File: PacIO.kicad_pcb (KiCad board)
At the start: 2 copper layers, 45.8 x 60 mm, 16 parts, among them J1 PacMan_Connector, J2 E-ink Display, J4 Charge_Indicator

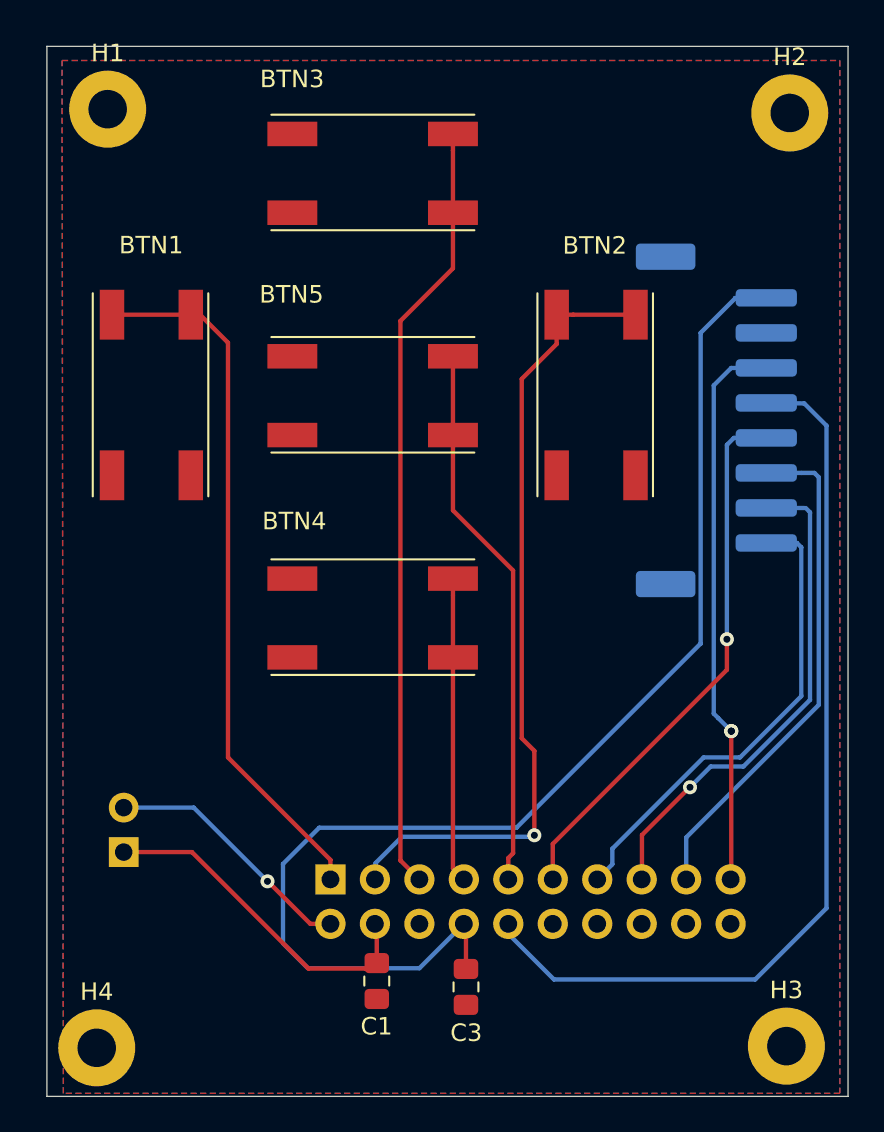
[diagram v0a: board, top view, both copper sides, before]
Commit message: Moved Parts Positions for final panel
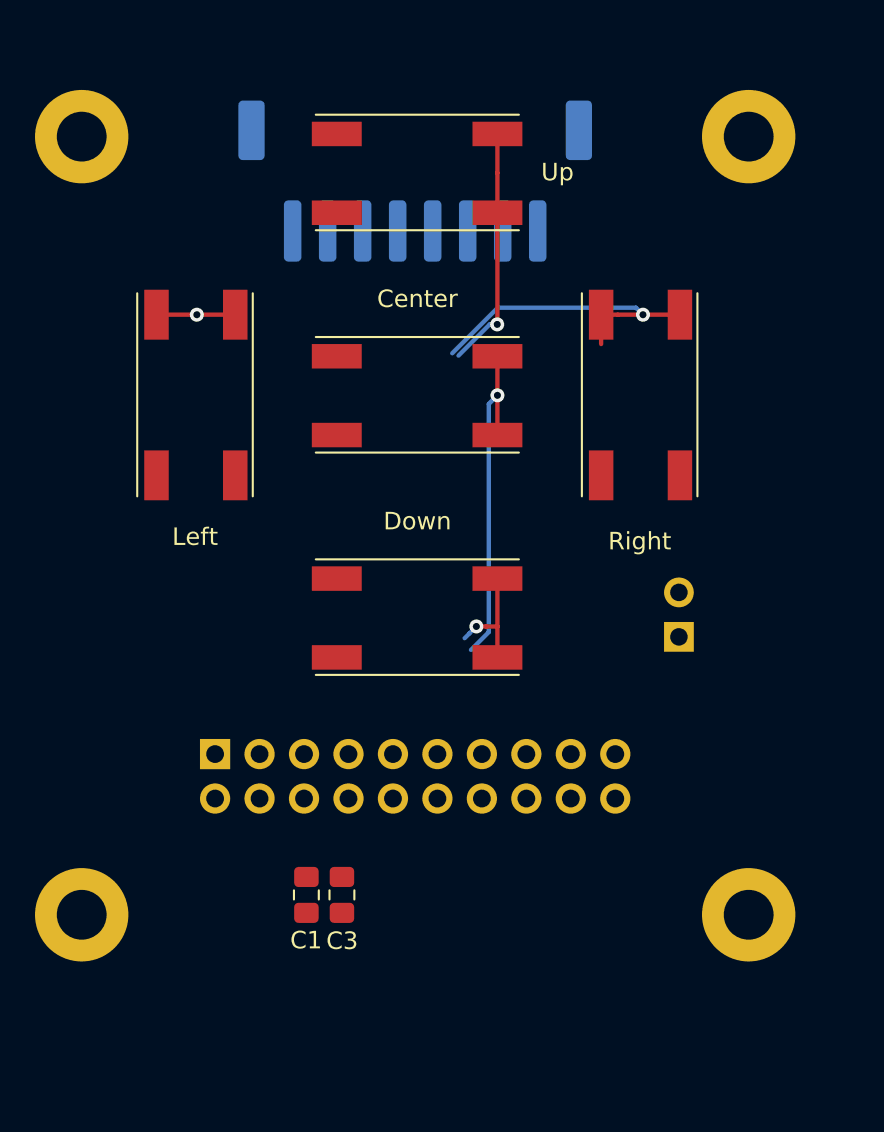
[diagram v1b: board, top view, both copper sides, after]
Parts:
- removed LOGO1: LafECEDepLogo, Lafayette_Electric_Car_Footprints:ECE_Logo_Jon
- H1, H2, H3, H4: footprint MountingHole:MountingHole_2.2mm_M2_Pad -> Lafayette_Electric_Car_Footprints:MountingHole_#4_Pad
- moved LOGO2 36.2 mm to (178.1, 109.3)
- moved J4 34.0 mm to (146.5, 126.4)
- moved J2 22.0 mm to (131.4, 100.3), turned to 0 degrees
- moved J1 9.73 mm to (120.0, 133.1)
- moved C3 8.82 mm to (127.3, 141.1)
- moved H3 7.81 mm to (150.5, 142.2)
- moved H4 7.65 mm to (112.4, 142.2)
- moved C1 6.35 mm to (125.2, 141.1)
- moved H2 2.71 mm to (150.5, 97.8)
- moved Center 2.54 mm to (131.6, 112.5)
- moved Down 2.54 mm to (131.6, 125.2)
- moved Up 2.54 mm to (131.6, 99.8)
- moved Left 2.54 mm to (118.9, 112.5)
- moved Right 2.54 mm to (144.3, 112.5)
- moved H1 2.16 mm to (112.4, 97.8)
- renumbered BTN5 to Center, BTN4 to Down, BTN1 to Left, BTN2 to Right, BTN3 to Up
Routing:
- net +3V3: track 70.6 -> 0.00 mm
- net /DISP_CLK: track 53.0 -> 0.00 mm
- net /BTN_LEFT: track 40.4 -> 5.03 mm, vias 0 -> 1
- net /DISP_DIN: track 32.8 -> 0.00 mm, vias 2 -> 0
- net /DISP_CS: track 31.4 -> 0.00 mm, vias 1 -> 0
- net /BTN_UP: track 44.3 -> 13.8 mm, vias 0 -> 1
- net /DISP_DC: track 29.2 -> 0.00 mm
- net /DISP_RST: track 28.5 -> 0.00 mm, vias 1 -> 0
- net /BTN_RIGHT: track 46.0 -> 18.3 mm
- net /DISP_BUSY: track 27.5 -> 0.00 mm
- net +24V: track 19.8 -> 0.00 mm
- net /CHRGE_LED: track 14.6 -> 0.00 mm, vias 1 -> 0
- net /BTN_CENTER: track 31.4 -> 19.7 mm, vias 0 -> 1
- net /BTN_DOWN: track 17.4 -> 6.63 mm, vias 0 -> 1
- removed copper zone on B.Cu, net GND
- removed copper zone on F.Cu, net GND
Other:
- board outline removed

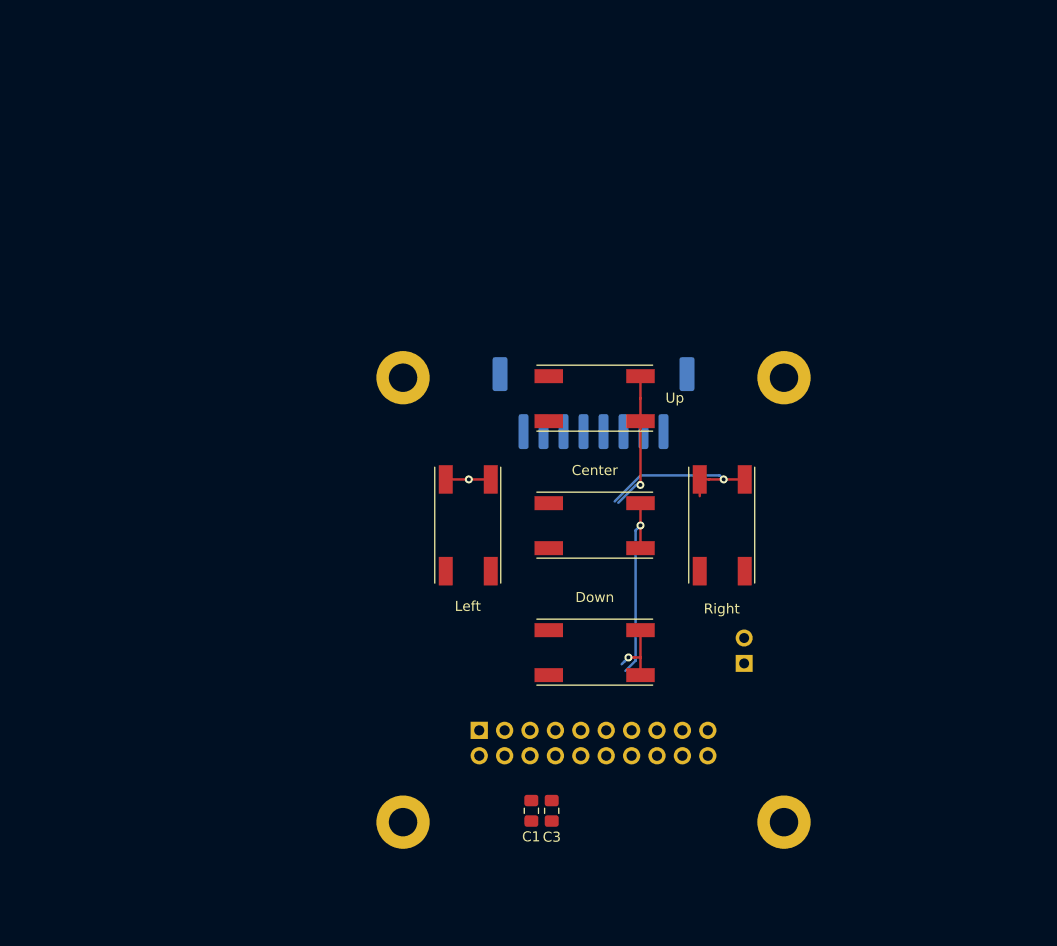
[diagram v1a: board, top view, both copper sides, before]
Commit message: Dimensions and Edge cuts
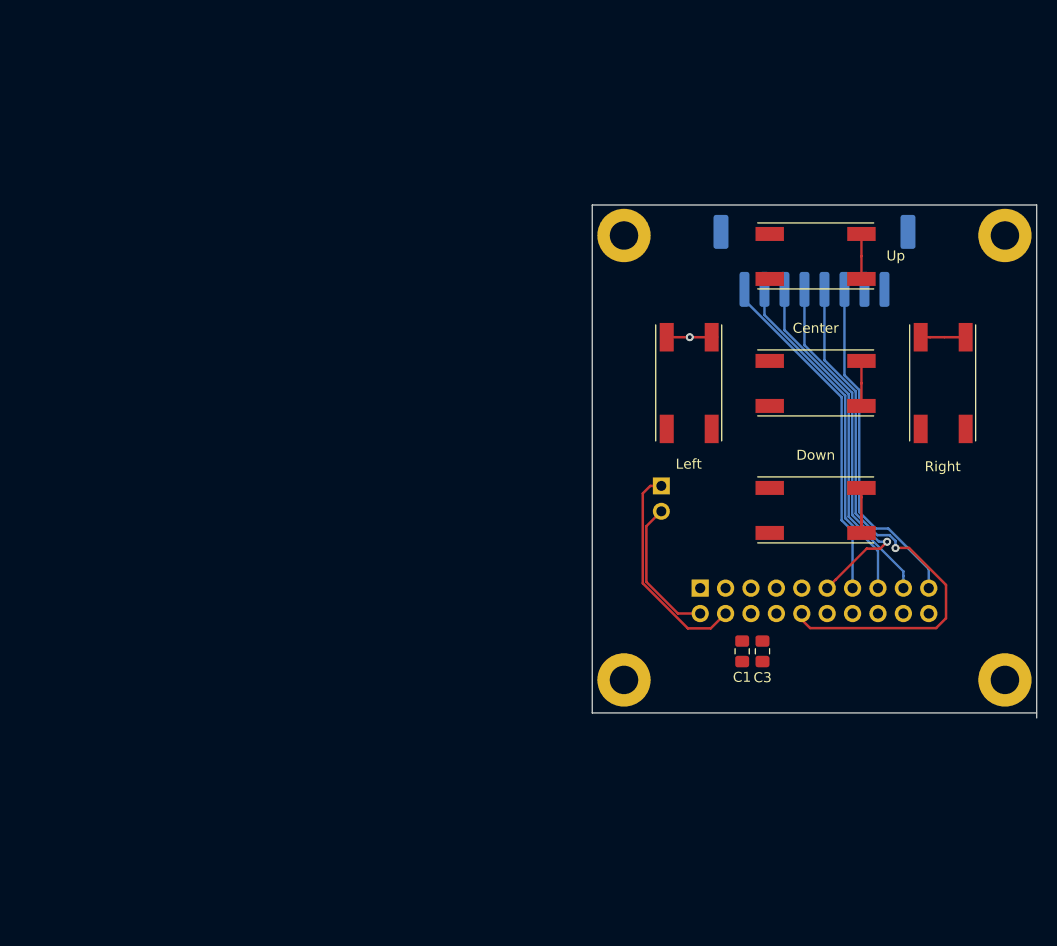
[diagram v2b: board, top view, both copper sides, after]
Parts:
- moved C1 26.4 mm to (146.3, 125.2)
- moved C3 26.4 mm to (148.3, 125.2)
- moved J2 26.3 mm to (153.5, 86.1)
- moved Left 26.3 mm to (141.0, 98.3)
- moved Right 26.3 mm to (166.4, 98.3)
- moved H4 26.3 mm to (134.5, 128.0)
- moved H1 26.3 mm to (134.5, 83.6)
- moved H3 26.3 mm to (172.6, 128.0)
- moved J1 26.3 mm to (142.1, 118.8)
- moved Center 26.3 mm to (153.7, 98.3)
- moved Down 26.3 mm to (153.7, 111.0)
- moved H2 26.3 mm to (172.6, 83.6)
- moved Up 26.3 mm to (153.7, 85.6)
- moved J4 19.6 mm to (138.2, 108.6), turned to 180 degrees
- moved LOGO2 12.5 mm to (165.6, 110.2)
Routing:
- net /DISP_CLK: track 0.00 -> 55.3 mm, vias 0 -> 1
- net /DISP_CS: track 0.00 -> 37.1 mm, vias 0 -> 1
- net /DISP_DC: track 0.00 -> 34.8 mm
- net /DISP_RST: track 0.00 -> 34.6 mm
- net /DISP_BUSY: track 0.00 -> 34.4 mm
- net /DISP_DIN: track 0.00 -> 34.1 mm
- net +24V: track 0.00 -> 21.9 mm
- net /BTN_CENTER: track 19.7 -> 4.50 mm, vias 1 -> 0
- net /CHRGE_LED: track 0.00 -> 14.4 mm
- net /BTN_RIGHT: track 18.3 -> 4.50 mm, vias 1 -> 0
- net /BTN_UP: track 13.8 -> 4.50 mm, vias 1 -> 0
- net /BTN_DOWN: track 6.63 -> 6.25 mm, vias 1 -> 0
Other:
- board outline added: 44.4 x 51.3 mm

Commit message: Routing
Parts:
- added LOGO1: LafECEDepLogo, Lafayette_Electric_Car_Footprints:ECE_Logo_Jon, F.Cu at (88.0, 66.3)
- J3: renamed from J4; value Charge_Indicator -> Charge LED; footprint Connector_PinSocket_2.54mm:PinSocket_1x02_P2.54mm_Vertical -> Lafayette_Electric_Car_Footprints:ScrewTerminal_0.2in
- moved J3 1.03 mm to (137.7, 109.5), turned to 270 degrees
- renumbered Left to BTN1, Right to BTN2, Up to BTN3, Down to BTN4, Center to BTN5
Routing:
- net +3V3: track 0.00 -> 61.3 mm, vias 0 -> 1
- net /BTN_RIGHT: track 4.50 -> 43.2 mm, vias 0 -> 1
- net /BTN_UP: track 4.50 -> 40.4 mm, vias 0 -> 1
- net /BTN_LEFT: track 5.03 -> 40.9 mm
- net /BTN_CENTER: track 4.50 -> 32.7 mm, vias 0 -> 1
- net /BTN_DOWN: track 6.25 -> 17.7 mm
- net +24V: track 21.9 -> 29.1 mm
- net /CHRGE_LED: track 14.4 -> 16.2 mm
- net /DISP_DIN: track 34.1 -> 33.4 mm
- added copper zone on B.Cu, net GND
- added copper zone on F.Cu, net GND
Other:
- board size 44.4 x 51.3 mm -> 44.4 x 50.8 mm
- board text added: "+"
- board text added: "-"
